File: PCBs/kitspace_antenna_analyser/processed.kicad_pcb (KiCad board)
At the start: 2 copper layers, 100 x 50 mm, 34 parts, among them IC1 MCP6002, IC2 ARDUINO_PRO_MINI_3.3V, P1 AD9850_CONN, P2 BNC, P3 CONN_LCD, P4 USB_OTG, P5 CONN_PROG, U1 AMS1117

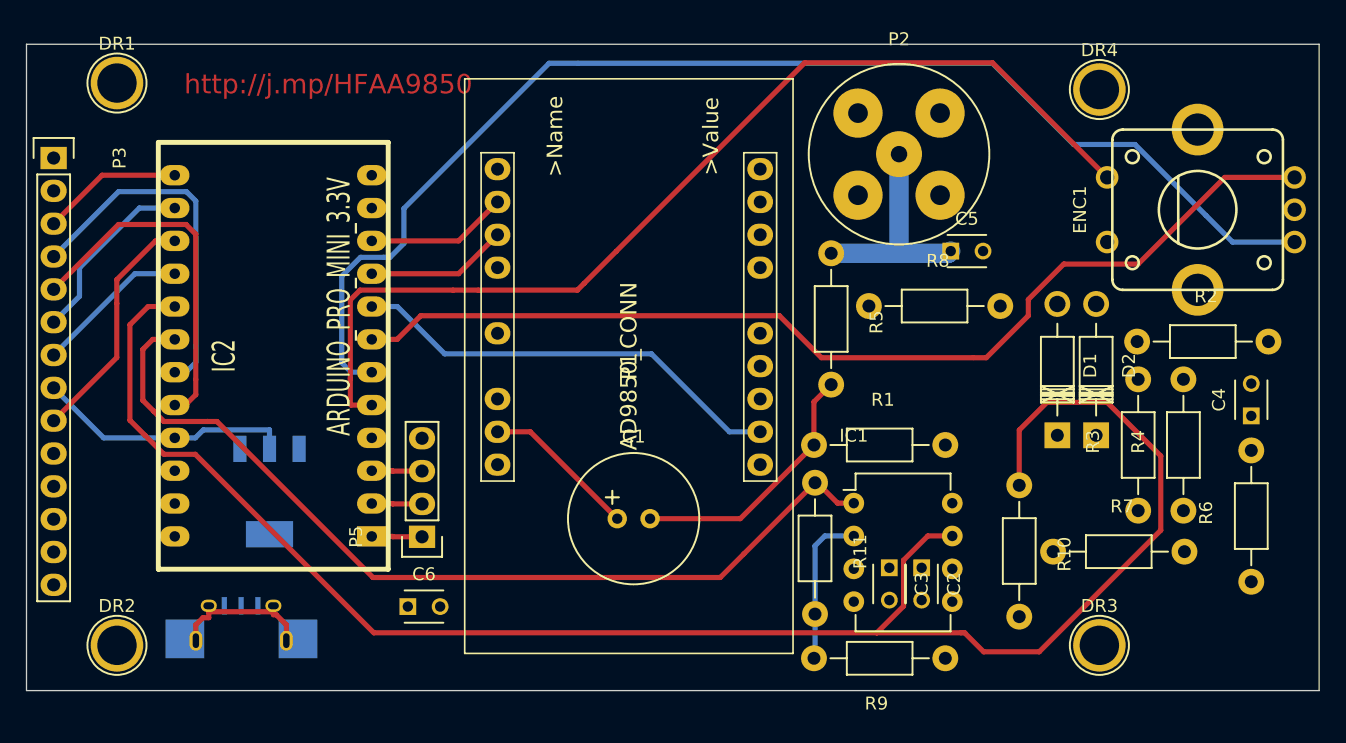
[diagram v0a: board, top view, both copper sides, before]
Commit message: recheck all circuits and clean up fill zone by rerouting the nets using freerouting and manually
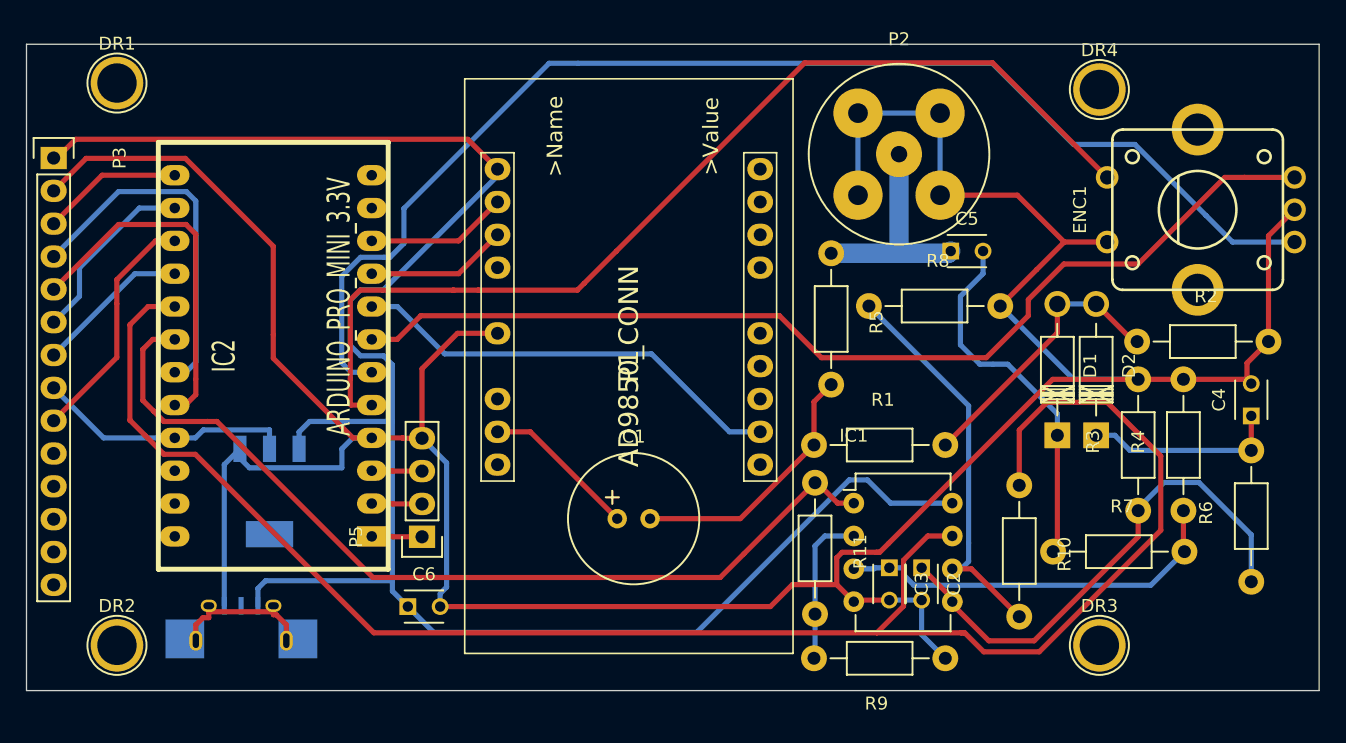
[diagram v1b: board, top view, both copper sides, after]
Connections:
- C2 pad 1: (no net) -> Net-(C2-Pad1)
- C2 pad 2: (no net) -> GND
- C3 pad 1: (no net) -> Net-(C3-Pad1)
- C3 pad 2: (no net) -> GND
- C4 pad 1: (no net) -> Net-(C4-Pad1)
- C4 pad 2: (no net) -> GND
- C5 pad 2: (no net) -> Net-(C5-Pad2)
- C6 pad 1: (no net) -> +5V
- C6 pad 2: (no net) -> GND
- D1 pad 1: (no net) -> Net-(C5-Pad2)
- D1 pad 2: (no net) -> Net-(D1-Pad2)
- D2 pad 1: (no net) -> Net-(C4-Pad1)
- D2 pad 2: (no net) -> Net-(D1-Pad2)
- ENC1 pad C: (no net) -> GND
- ENC1 pad SW1: (no net) -> GND
- IC1 pad 3: (no net) -> Net-(C3-Pad1)
- IC1 pad 4: (no net) -> GND
- IC1 pad 5: (no net) -> Net-(C2-Pad1)
- IC1 pad 6: (no net) -> Net-(IC1-Pad6)
- IC1 pad 8: (no net) -> +5V
- IC2 pad 11: (no net) -> Net-(IC2-Pad11)
- IC2 pad 12: (no net) -> Net-(IC2-Pad12)
- IC2 pad 22: (no net) -> Net-(IC2-Pad22)
- IC2 pad 23: (no net) -> Net-(IC2-Pad23)
- IC2 pad 24: (no net) -> Net-(IC2-Pad24)
- IC2 pad 4: (no net) -> GND
- P1 pad 1: (no net) -> +5V
- P1 pad 10: (no net) -> Net-(P1-Pad10)
- P1 pad 11: (no net) -> Net-(P1-Pad11)
- P1 pad 13: (no net) -> Net-(P1-Pad13)
- P1 pad 14: (no net) -> Net-(P1-Pad14)
- P1 pad 15: (no net) -> Net-(P1-Pad15)
- P1 pad 17: (no net) -> Net-(P1-Pad17)
- P1 pad 18: (no net) -> Net-(P1-Pad18)
- P1 pad 19: (no net) -> Net-(P1-Pad19)
- P1 pad 20: (no net) -> Net-(P1-Pad20)
- P1 pad 4: (no net) -> Net-(P1-Pad4)
- P1 pad 6: (no net) -> GND
- P1 pad 8: (no net) -> Net-(P1-Pad8)
- P2 pad 2: (no net) -> GND
- P3 pad 1: (no net) -> +5V
- P3 pad 10: (no net) -> Net-(P3-Pad10)
- P3 pad 11: (no net) -> Net-(P3-Pad11)
- P3 pad 12: (no net) -> Net-(P3-Pad12)
- P3 pad 13: (no net) -> Net-(P3-Pad13)
- P3 pad 14: (no net) -> Net-(P3-Pad14)
- P3 pad 2: (no net) -> GND
- P4 pad 1: (no net) -> +5V
- P4 pad 3: (no net) -> Net-(P4-Pad3)
- P4 pad 5: (no net) -> GND
- P5 pad 4: (no net) -> GND
- R1 pad 2: (no net) -> Net-(D1-Pad2)
- R10 pad 2: (no net) -> Net-(IC1-Pad6)
- R2 pad 1: (no net) -> Net-(D1-Pad2)
- R2 pad 2: (no net) -> GND
- R3 pad 1: (no net) -> Net-(C2-Pad1)
- R3 pad 2: (no net) -> GND
- R4 pad 1: (no net) -> Net-(C3-Pad1)
- R4 pad 2: (no net) -> GND
- R6 pad 1: (no net) -> Net-(C2-Pad1)
- R6 pad 2: (no net) -> Net-(C4-Pad1)
- R7 pad 1: (no net) -> Net-(C5-Pad2)
- R7 pad 2: (no net) -> Net-(C3-Pad1)
- R8 pad 1: (no net) -> Net-(IC1-Pad6)
- R8 pad 2: (no net) -> GND
- R9 pad 1: (no net) -> GND
- U1 pad 1: (no net) -> GND
- U1 pad 3: (no net) -> +5V
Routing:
- net GND: track 0.00 -> 248.8 mm
- net +5V: track 0.00 -> 147.8 mm
- net Net-(C2-Pad1): track 0.00 -> 40.4 mm
- net Net-(IC1-Pad6): track 0.00 -> 31.2 mm
- net Net-(C3-Pad1): track 0.00 -> 30.8 mm
- net Net-(C5-Pad2): track 0.00 -> 28.5 mm
- net Net-(D1-Pad2): track 0.00 -> 21.9 mm
- net Net-(C4-Pad1): track 0.00 -> 15.2 mm
- net Net-(IC2-Pad8): track 34.1 -> 35.0 mm
- net Net-(IC1-Pad1): track 71.1 -> 71.6 mm
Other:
- board text removed: "http://j.mp/HFAA9850"

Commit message: clean psbc that are missed before
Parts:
- gave numbers to parts that had none: 2
